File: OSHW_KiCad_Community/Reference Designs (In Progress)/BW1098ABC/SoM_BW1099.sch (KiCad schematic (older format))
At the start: 26 parts, among them J1 20021121-00010T1LF, J2 20021121-00010T1LF, J3 DF40HC(3.0)-100DS-0.4V_BW1099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, J4 20021121-00010T1LF, Q1 RE1C002UNTCL, Q2 RE1C002UNTCL, Q3 RE1C002UNTCL

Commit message: BW1098ABC - added back in usbc, got rid of hierarchical labeling in favor of globals. Passes ERC
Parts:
- removed C1: 4.7UF0603, Capacitor_SMD:C_0603_1608Metric, symbol BW1098ABC-rescue:4.7UF0603-SparkFun-Capacitors
- MISC1: symbol depthAI_sch:Layout_Guide_BW1099 -> DEPTH:Layout_Guide_BW1099
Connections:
- net labels added: MIPI_RX5_D0_N, MIPI_RX5_D0_P, MIPI_RX5_D1_N, MIPI_RX5_D1_P, USB_D_N, USB_D_P, USB_RX_N, USB_RX_P, USB_TX_N, USB_TX_P, VBUS
- net labels removed: CTL_CAM_A, CTL_CAM_B, I2C1, I2C2, MIPI_CAM_B, MIPI_CAM_C, VDD_5V, nMR
- wire segments 198 -> 192
- no-connect marks 6 -> 0
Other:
- note removed: "Code executed when PMS150C comes out of RST \n(PRST#), toggling RST_1 as required"
- note removed: "PMS150C powered by 5V\nso that it is the first in the \npower sequence to turn on"

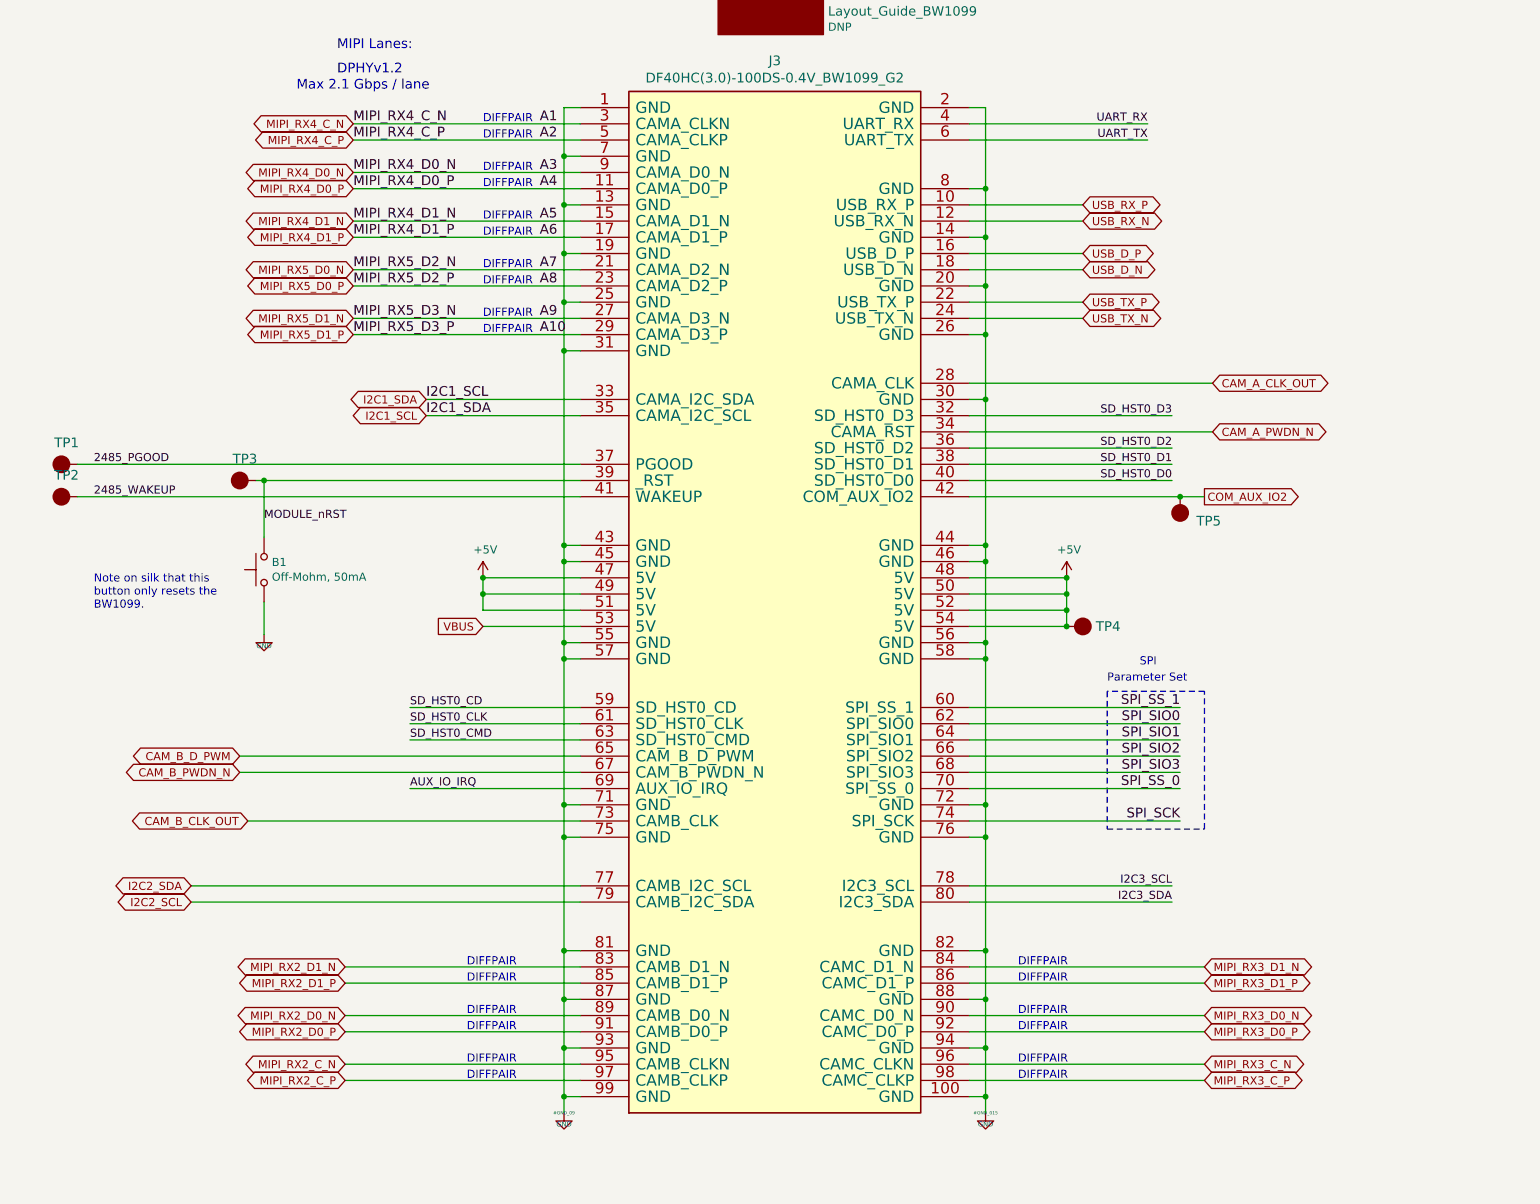
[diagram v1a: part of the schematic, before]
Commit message: going through footprints and datasheet stuff
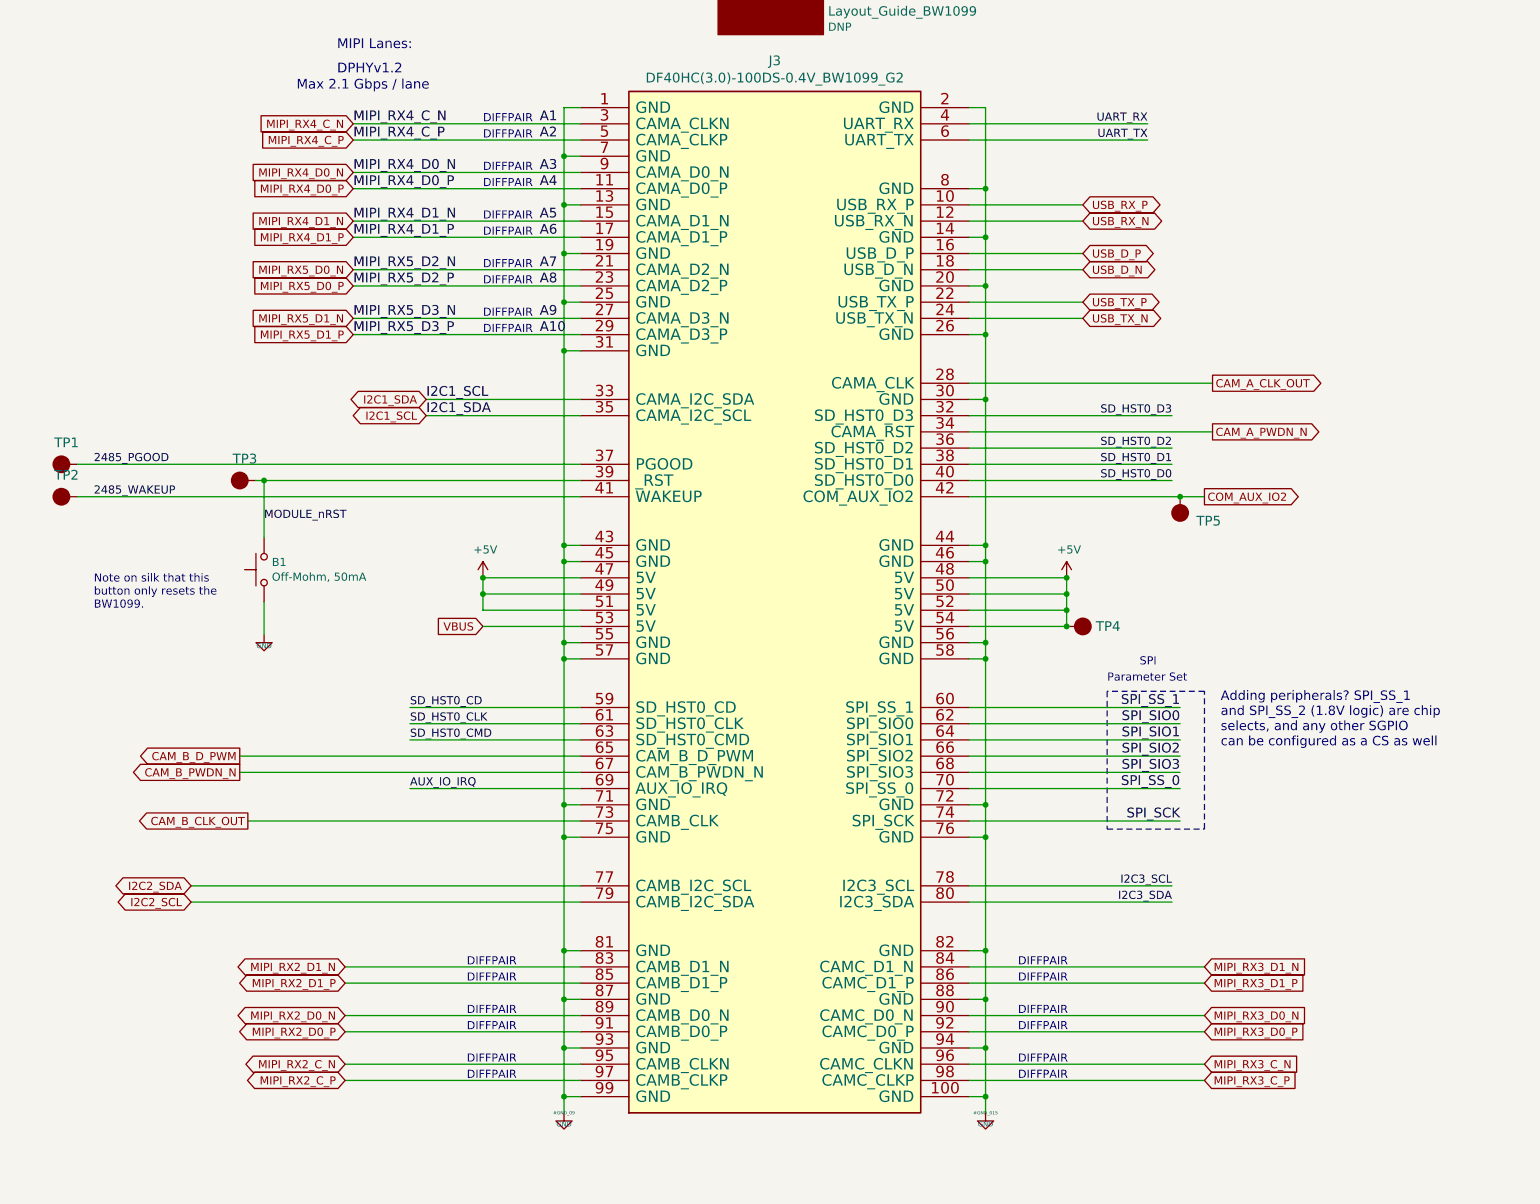
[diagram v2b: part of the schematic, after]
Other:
- note added: "Adding peripherals? SPI_SS_1\nand SPI_SS_2 (1.8V logic) are chip\nselects, and any other SGPIO\ncan be configured as a CS as well"
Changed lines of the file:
@@
 Wire Wire Line
 	7000 7050 9100 7050
-Text GLabel 7700 3050 0    50   BiDi ~ 0
-MIPI_RX4_C_N
-Text GLabel 7700 3150 0    50   BiDi ~ 0
-MIPI_RX4_C_P
-Text GLabel 7700 3350 0    50   BiDi ~ 0
+Text GLabel 7700 3350 0    50   Input ~ 0
 MIPI_RX4_D0_N
-Text GLabel 7700 3450 0    50   BiDi ~ 0
+Text GLabel 7700 3450 0    50   Input ~ 0
 MIPI_RX4_D0_P
-Text GLabel 7700 3650 0    50   BiDi ~ 0
+Text GLabel 7700 3650 0    50   Input ~ 0
 MIPI_RX4_D1_N
-Text GLabel 7700 3750 0    50   BiDi ~ 0
+Text GLabel 7700 3750 0    50   Input ~ 0
 MIPI_RX4_D1_P
-Text GLabel 7700 3950 0    50   BiDi ~ 0
+Text GLabel 7700 3950 0    50   Input ~ 0
 MIPI_RX5_D0_N
-Text GLabel 7700 4050 0    50   BiDi ~ 0
+Text GLabel 7700 4050 0    50   Input ~ 0
 MIPI_RX5_D0_P
-Text GLabel 7700 4250 0    50   BiDi ~ 0
+Text GLabel 7700 4250 0    50   Input ~ 0
 MIPI_RX5_D1_N
-Text GLabel 7700 4350 0    50   BiDi ~ 0
+Text GLabel 7700 4350 0    50   Input ~ 0
 MIPI_RX5_D1_P
 Text GLabel 12950 5350 2    50   Output ~ 0
 COM_AUX_IO2
-Text GLabel 12950 8250 2    50   BiDi ~ 0
+Text GLabel 12950 8250 2    50   Input ~ 0
 MIPI_RX3_D1_N
-Text GLabel 12950 8350 2    50   BiDi ~ 0
+Text GLabel 12950 8350 2    50   Input ~ 0
 MIPI_RX3_D1_P
-Text GLabel 12950 8550 2    50   BiDi ~ 0
+Text GLabel 12950 8550 2    50   Input ~ 0
 MIPI_RX3_D0_N
-Text GLabel 12950 8650 2    50   BiDi ~ 0
+Text GLabel 12950 8650 2    50   Input ~ 0
 MIPI_RX3_D0_P
-Text GLabel 12950 8850 2    50   BiDi ~ 0
+Text GLabel 12950 8850 2    50   Input ~ 0
 MIPI_RX3_C_N
-Text GLabel 12950 8950 2    50   BiDi ~ 0
+Text GLabel 12950 8950 2    50   Input ~ 0
 MIPI_RX3_C_P
 Text GLabel 7650 8250 0    50   BiDi ~ 0
@@
 Text GLabel 12200 4150 2    50   BiDi ~ 0
 USB_TX_P
-Text GLabel 13000 4950 2    50   BiDi ~ 0
+Text GLabel 13000 4950 2    50   Output ~ 0
 CAM_A_PWDN_N
-Text GLabel 13000 4650 2    50   BiDi ~ 0
+Text GLabel 13000 4650 2    50   Output ~ 0
 CAM_A_CLK_OUT
 Text GLabel 6700 7750 0    50   BiDi ~ 0
@@
 Text GLabel 6700 7850 0    50   BiDi ~ 0
 I2C2_SCL
-Text GLabel 7000 6950 0    50   BiDi ~ 0
-CAM_B_D_PWM
-Text GLabel 7000 7050 0    50   BiDi ~ 0
+Text GLabel 7000 7050 0    50   Output ~ 0
 CAM_B_PWDN_N
-Text GLabel 7050 7350 0    50   BiDi ~ 0
+Text GLabel 7050 7350 0    50   Output ~ 0
 CAM_B_CLK_OUT
 Wire Wire Line
@@
 Text Label 12600 3050 2    50   ~ 0
 UART_RX
+Text GLabel 7700 3150 0    50   Input ~ 0
+MIPI_RX4_C_P
+Text GLabel 7700 3050 0    50   Input ~ 0
+MIPI_RX4_C_N
+Text GLabel 7000 6950 0    50   Output ~ 0
+CAM_B_D_PWM
+Text Notes 13050 6900 0    58   ~ 0
+Adding peripherals? SPI_SS_1\nand SPI_SS_2 (1.8V logic) are chip\nselects, and any other SGPIO\ncan be configured as a CS as well
 $EndSCHEMATC

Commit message: both camera connector footprints completed
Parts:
- H5, H6, H7, H8: footprint fp_luxonis:Mounting_Wuerth_WA-SMSI-M2_H3mm_9774030243 -> Mounting_Wuerth:Mounting_Wuerth_WA-SMSI-M2_H3mm_9774030243
- J3: footprint fp_luxonis:HRS_DF40HC(3.0)-100DS-0.4V(58 -> Luxonis_Kicad_Master:DF40HC(3.0)-100DS-0.4V(58)
- MISC1: footprint fp_luxonis:BW1099_Layout_Guide -> Luxonis_Kicad_Master:BW1099_Layout_Guide; symbol DEPTH:Layout_Guide_BW1099 -> BW1098ABC-rescue:Layout_Guide_BW1099-DEPTH
- Q1, Q2, Q3: footprint OSHW_LuxonisMaster_20201223:RE1C002UNTCL -> (none)
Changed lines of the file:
@@
 F 0 "H7" H 10450 1899 50  0000 L CNN
 F 1 "MountingHole_Pad" H 10550 1800 50  0001 L CNN
-F 2 "fp_luxonis:Mounting_Wuerth_WA-SMSI-M2_H3mm_9774030243" H 10350 1850 50  0001 C CNN
+F 2 "Mounting_Wuerth:Mounting_Wuerth_WA-SMSI-M2_H3mm_9774030243" H 10350 1850 50  0001 C CNN
 F 3 "~" H 10350 1850 50  0001 C CNN
 	1    10350 1850
@@
 F 0 "H6" H 10100 1899 50  0000 L CNN
 F 1 "MountingHole_Pad" H 10200 1800 50  0001 L CNN
-F 2 "fp_luxonis:Mounting_Wuerth_WA-SMSI-M2_H3mm_9774030243" H 10000 1850 50  0001 C CNN
+F 2 "Mounting_Wuerth:Mounting_Wuerth_WA-SMSI-M2_H3mm_9774030243" H 10000 1850 50  0001 C CNN
 F 3 "~" H 10000 1850 50  0001 C CNN
 	1    10000 1850
@@
 F 0 "H5" H 9750 1899 50  0000 L CNN
 F 1 "MountingHole_Pad" H 9850 1800 50  0001 L CNN
-F 2 "fp_luxonis:Mounting_Wuerth_WA-SMSI-M2_H3mm_9774030243" H 9650 1850 50  0001 C CNN
+F 2 "Mounting_Wuerth:Mounting_Wuerth_WA-SMSI-M2_H3mm_9774030243" H 9650 1850 50  0001 C CNN
 F 3 "~" H 9650 1850 50  0001 C CNN
 	1    9650 1850
@@
 F 0 "H8" H 10800 1899 50  0000 L CNN
 F 1 "MountingHole_Pad" H 10900 1800 50  0001 L CNN
-F 2 "fp_luxonis:Mounting_Wuerth_WA-SMSI-M2_H3mm_9774030243" H 10700 1850 50  0001 C CNN
+F 2 "Mounting_Wuerth:Mounting_Wuerth_WA-SMSI-M2_H3mm_9774030243" H 10700 1850 50  0001 C CNN
 F 3 "~" H 10700 1850 50  0001 C CNN
 	1    10700 1850
@@
 F 0 "Q3" H 2005 8296 50  0000 L CNN
 F 1 "RE1C002UNTCL" H 2005 8205 50  0000 L CNN
-F 2 "OSHW_LuxonisMaster_20201223:RE1C002UNTCL" H 2000 8350 50  0001 C CNN
+F 2 "" H 2000 8350 50  0001 C CNN
 F 3 "~" H 1800 8250 50  0001 C CNN
 	1    1800 8250
@@
 F 0 "Q2" H 1955 6446 50  0000 L CNN
 F 1 "RE1C002UNTCL" H 1955 6355 50  0000 L CNN
-F 2 "OSHW_LuxonisMaster_20201223:RE1C002UNTCL" H 1950 6500 50  0001 C CNN
+F 2 "" H 1950 6500 50  0001 C CNN
 F 3 "~" H 1750 6400 50  0001 C CNN
 	1    1750 6400
@@
 F 0 "Q1" H 1955 4146 50  0000 L CNN
 F 1 "RE1C002UNTCL" H 1955 4055 50  0000 L CNN
-F 2 "OSHW_LuxonisMaster_20201223:RE1C002UNTCL" H 1950 4200 50  0001 C CNN
+F 2 "" H 1950 4200 50  0001 C CNN
 F 3 "~" H 1750 4100 50  0001 C CNN
 	1    1750 4100
@@
 F 0 "J3" H 10300 3239 60  0000 C CNN
 F 1 "DF40HC(3.0)-100DS-0.4V_BW1099_G2" H 10300 3133 60  0000 C CNN
-F 2 "fp_luxonis:HRS_DF40HC(3.0)-100DS-0.4V(58" H 9100 2950 60  0001 C CNN
+F 2 "Luxonis_Kicad_Master:DF40HC(3.0)-100DS-0.4V(58)" H 9100 2950 60  0001 C CNN
 F 3 "https://www.hirose.com/product/document?clcode=CL0684-4003-3-51&productname=DF40C-60DP-0.4V(51)&series=DF40&documenttype=Catalog&lang=en&documentid=D31649_en" H 9100 2950 60  0001 C CNN
 	1    9100 2950
@@
 	12800 5350 12950 5350
 $Comp
-L DEPTH:Layout_Guide_BW1099 MISC1
+L BW1098ABC-rescue:Layout_Guide_BW1099-DEPTH MISC1
 U 1 1 6017E490
 P 10350 2350
 F 0 "MISC1" H 10628 2447 58  0000 L CNN
 F 1 "Layout_Guide_BW1099" H 10628 2344 58  0000 L CNN
-F 2 "fp_luxonis:BW1099_Layout_Guide" H 10050 2750 58  0001 C CNN
+F 2 "Luxonis_Kicad_Master:BW1099_Layout_Guide" H 10050 2750 58  0001 C CNN
 F 3 "" H 10050 2750 58  0001 C CNN
 F 4 "DNP" H 10628 2247 50  0000 L CNN "Population"

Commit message: finished and checked both camera connectors for the BW1098
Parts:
- B1: footprint DTSM-32N-V-T_R:DTSM32NVTR -> Luxonis_Kicad_Master:DTSM32NVTR
- D1: footprint Diode_SMD:D_0201_0603Metric -> Diode_SMD:D_0603_1608Metric
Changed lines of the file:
@@
 F 0 "B1" V 7196 5752 50  0000 R CNN
 F 1 "Off-Mohm, 50mA" V 7105 5752 50  0000 R CNN
-F 2 "DTSM-32N-V-T_R:DTSM32NVTR" H 7150 6000 50  0001 C CNN
+F 2 "Luxonis_Kicad_Master:DTSM32NVTR" H 7150 6000 50  0001 C CNN
 F 3 "http://www.apem.com/int/index.php?controller=attachment&id_attachment=488" H 7150 6000 50  0001 C CNN
 	1    7150 5800
@@
 F 0 "D1" V 1889 3482 50  0000 R CNN
 F 1 "RED0603" V 1798 3482 50  0000 R CNN
-F 2 "Diode_SMD:D_0201_0603Metric" H 1850 3600 50  0001 C CNN
+F 2 "Diode_SMD:D_0603_1608Metric" H 1850 3600 50  0001 C CNN
 F 3 "~" H 1850 3600 50  0001 C CNN
 	1    1850 3600
